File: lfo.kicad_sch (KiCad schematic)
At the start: 3 parts

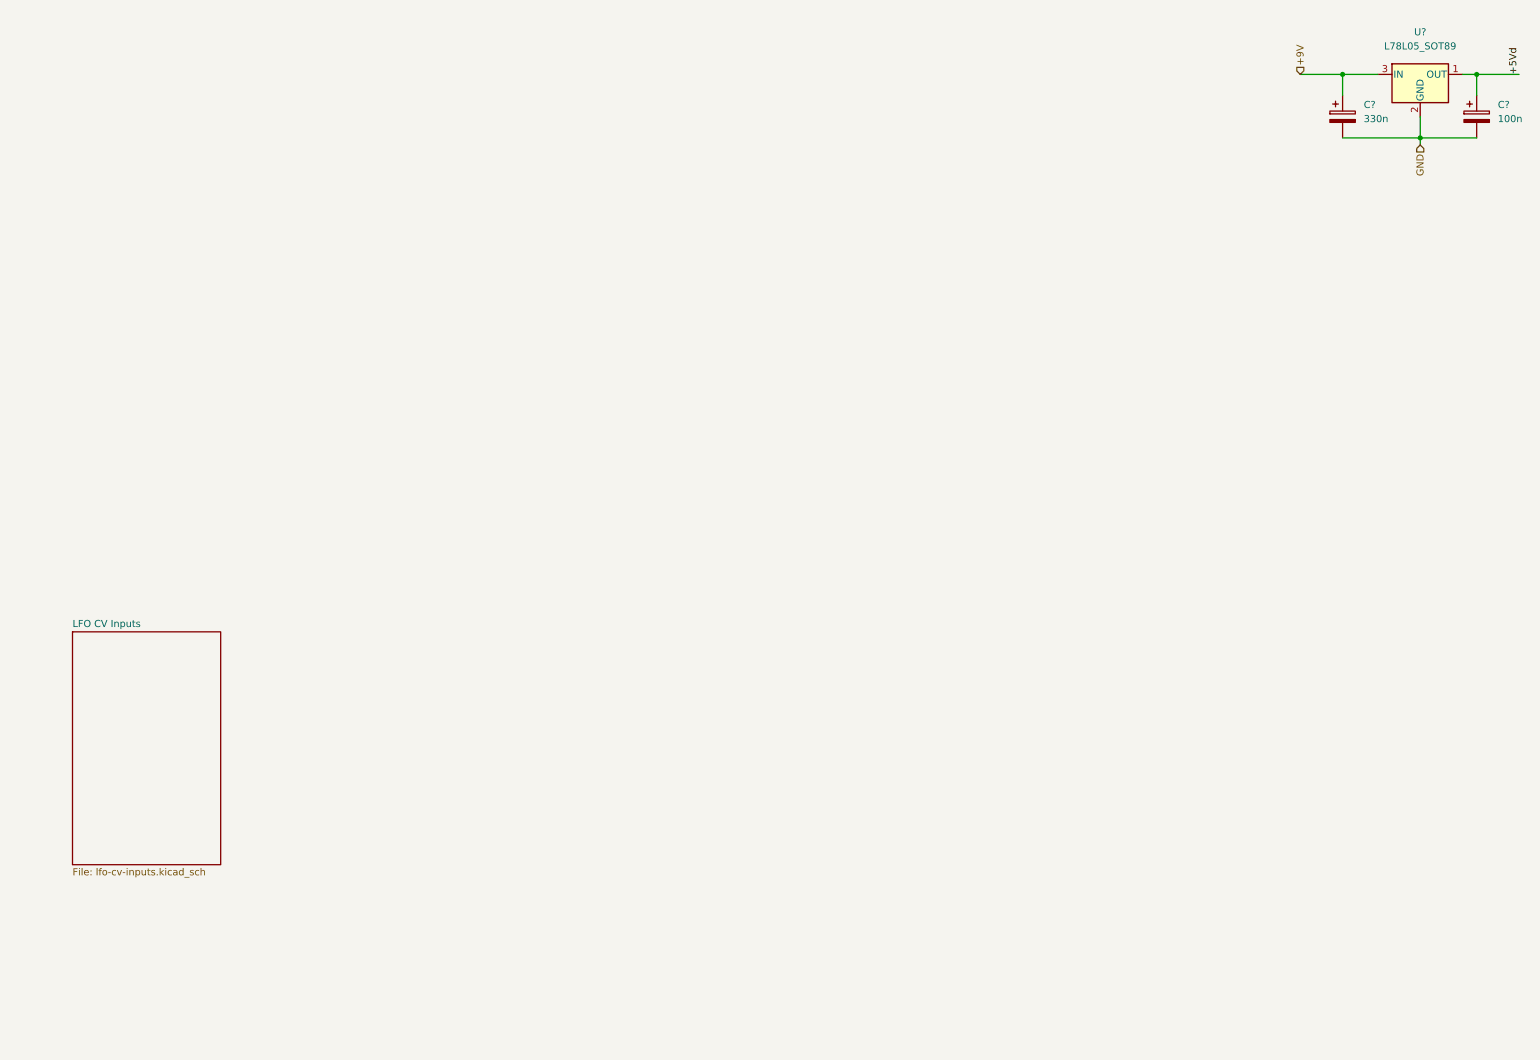
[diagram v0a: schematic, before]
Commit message: LFO schem capture done / replace r2r opamps
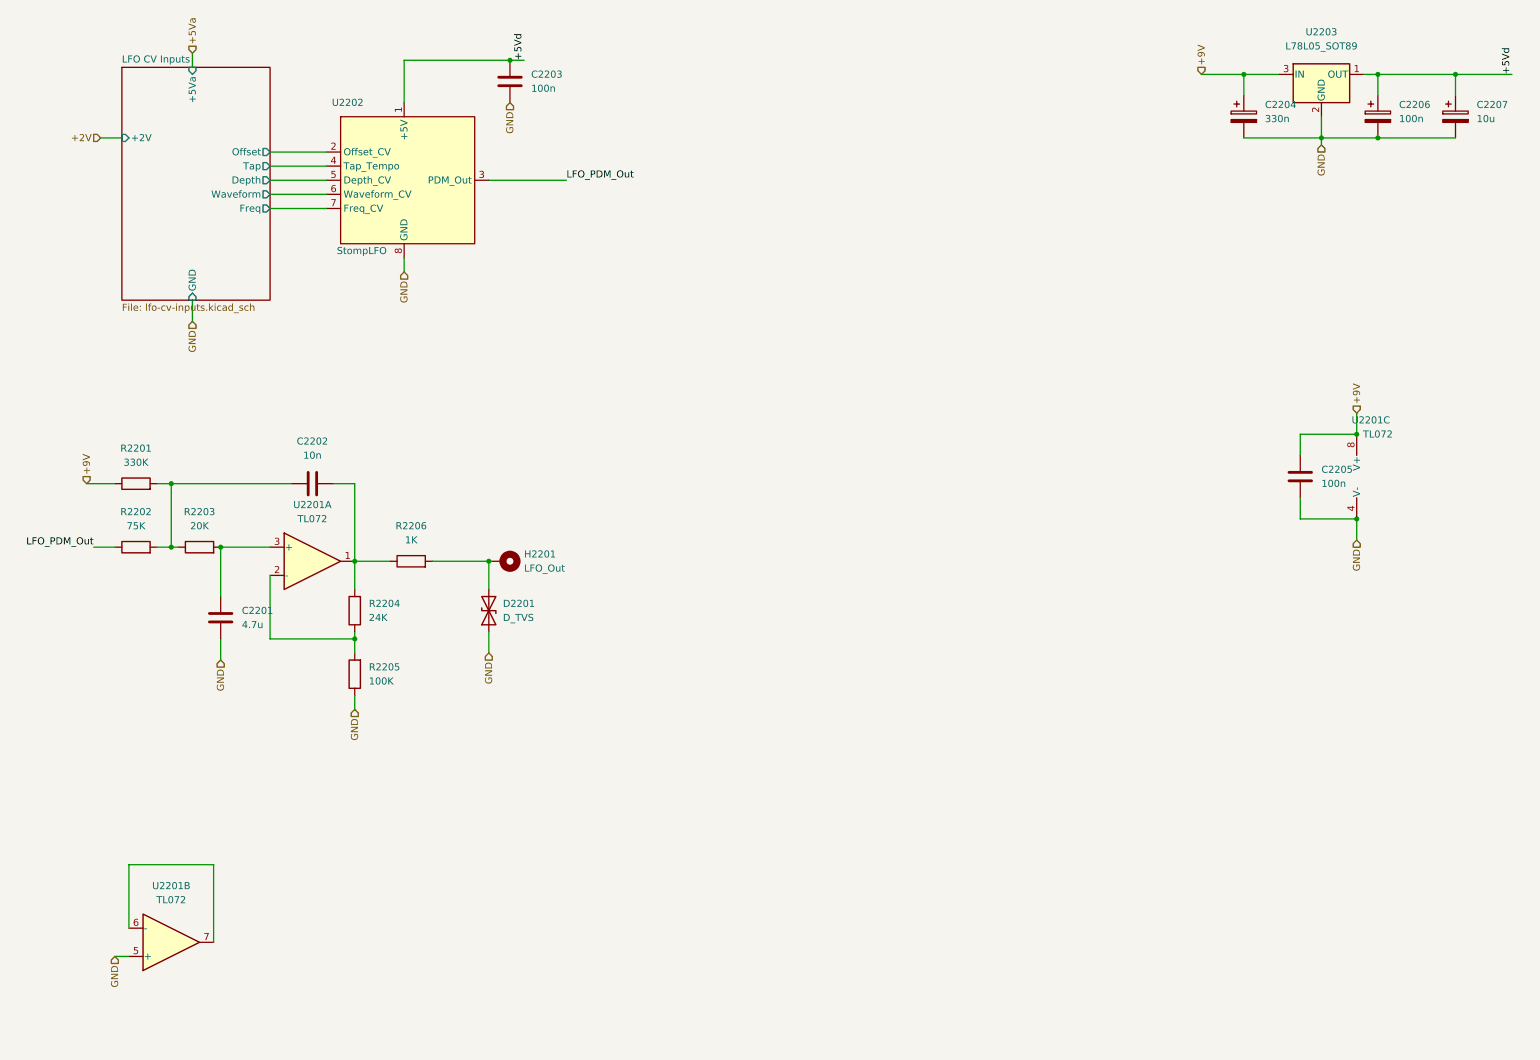
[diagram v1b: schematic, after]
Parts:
- added C2201: 4.7u, Capacitor_SMD:C_0603_1608Metric_Pad1.08x0.95mm_HandSolder, symbol Device:C
- added C2202: 10n, Capacitor_SMD:C_0603_1608Metric_Pad1.08x0.95mm_HandSolder, symbol Device:C
- added C2203, C2205: 100n, Capacitor_SMD:C_0603_1608Metric_Pad1.08x0.95mm_HandSolder, symbol Device:C
- added C2207: 10u, Capacitor_SMD:CP_Elec_4x5.4, symbol Device:C_Polarized
- added D2201: D_TVS, Diode_SMD:D_SOD-323_HandSoldering, symbol Device:D_TVS
- added H2201: LFO_Out, MountingHole:MountingHole_4.3mm_M4_Pad_TopBottom, symbol Mechanical:MountingHole_Pad
- added R2201: 330K, Resistor_SMD:R_0603_1608Metric_Pad0.98x0.95mm_HandSolder, symbol Device:R
- added R2202: 75K, Resistor_SMD:R_0603_1608Metric_Pad0.98x0.95mm_HandSolder, symbol Device:R
- added R2203: 20K, Resistor_SMD:R_0603_1608Metric_Pad0.98x0.95mm_HandSolder, symbol Device:R
- added R2204: 24K, Resistor_SMD:R_0603_1608Metric_Pad0.98x0.95mm_HandSolder, symbol Device:R
- added R2205: 100K, Resistor_SMD:R_0603_1608Metric_Pad0.98x0.95mm_HandSolder, symbol Device:R
- added R2206: 1K, Resistor_SMD:R_0603_1608Metric_Pad0.98x0.95mm_HandSolder, symbol Device:R
- added U2201: TL072, Package_SO:SOIC-8_3.9x4.9mm_P1.27mm, symbol Amplifier_Operational:TL072
- added U2202: StompLFO, Package_DIP:DIP-8_W7.62mm, symbol stomplfo:StompLFO
- gave numbers to parts that had none: 3
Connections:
- net +5Vd: now also C2203.1, C2207.1, U2202.1 (+5V)
- net +9V: now also C2205.1, R2201.1, U2201.8 (V+)
- net GND: now also C2201.2, C2203.2, C2205.2, C2207.2, D2201.1 (A1), R2205.1, U2201.4 (V-), U2201.5 (+), U2202.8 (GND)
- new net: R2204.1, R2205.2, U2201.2 (-)
- new net: C2202.1, R2201.2, R2202.2, R2203.1
- new net: U2201.6 (-), U2201.7
- new net: C2202.2, R2204.2, R2206.1, U2201.1
- new net: D2201.2 (A2), H2201.1, R2206.2
- new net: C2201.1, R2203.2, U2201.3 (+)
- new net LFO CV Inputs/Depth: U2202.5 (Depth_CV)
- new net LFO CV Inputs/Freq: U2202.7 (Freq_CV)
- new net LFO CV Inputs/Offset: U2202.2 (Offset_CV)
- new net LFO CV Inputs/Tap: U2202.4 (Tap_Tempo)
- new net LFO CV Inputs/Waveform: U2202.6 (Waveform_CV)
- new net LFO_PDM_Out: R2202.1, U2202.3 (PDM_Out)
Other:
- sheet LFO CV Inputs ports: added +2V, +5Va, Depth, Freq, GND, Offset, Tap, Waveform; removed none
- moved on the sheet: C2204, C2206, U2203

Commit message: LFO layout down
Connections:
- net GND: now also U2201.3 (+); no longer U2201.5 (+)
- net at R2204.1, R2205.2: now also U2201.6 (-); no longer U2201.2 (-)
- net at C2202.2, R2204.2, R2206.1: now also U2201.7; no longer U2201.1
- net at C2201.1, R2203.2: now also U2201.5 (+); no longer U2201.3 (+)
- new net: U2201.1, U2201.2 (-)
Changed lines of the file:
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@@
     (pin "2")
   )
-  (symbol (lib_id "Amplifier_Operational:TL072") (at 39.37 179.07 0) (mirror x) (unit 2)
+  (symbol (lib_id "Amplifier_Operational:TL072") (at 39.37 179.07 0) (mirror x) (unit 1)
     (in_bom yes) (on_board yes) (fields_autoplaced)
     (property "Reference" "U2201" (id 0) (at 39.37 168.91 0))
@@
     (pin "2")
   )
-  (symbol (lib_id "Amplifier_Operational:TL072") (at 64.77 110.49 0) (unit 1)
+  (symbol (lib_id "Amplifier_Operational:TL072") (at 64.77 110.49 0) (unit 2)
     (in_bom yes) (on_board yes) (fields_autoplaced)
     (property "Reference" "U2201" (id 0) (at 64.77 100.33 0))

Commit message: Relay switch schem capture done
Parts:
- added C2208: 100n, Capacitor_SMD:C_0603_1608Metric_Pad1.08x0.95mm_HandSolder, symbol Device:C
- added C2209: 4.7u, Capacitor_SMD:C_0603_1608Metric_Pad1.08x0.95mm_HandSolder, symbol Device:C
- added R2207, R2208: 20K, Resistor_SMD:R_0603_1608Metric_Pad0.98x0.95mm_HandSolder, symbol Device:R
- added R2209, R2210: 10K, Resistor_SMD:R_0603_1608Metric_Pad0.98x0.95mm_HandSolder, symbol Device:R
- added R2211: 100, Resistor_SMD:R_0603_1608Metric_Pad0.98x0.95mm_HandSolder, symbol Device:R
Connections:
- net +2V: now also C2208.1, C2209.1, R2211.2
- net +5Va: now also R2207.1
- net +9V: now also R2208.1
- net GND: now also C2208.2, C2209.2, R2209.1; no longer U2201.3 (+)
- net at U2201.2 (-): now also R2207.2, R2210.1; no longer U2201.1
- new net: R2210.2, R2211.1, U2201.1
- new net: R2208.2, R2209.2, U2201.3 (+)
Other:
- moved on the sheet: U2201A

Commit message: PSU schem capture done
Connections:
- net +9V: no longer C2204.1, U2203.3 (IN)
- new net +9Vd: C2204.1, U2203.3 (IN)
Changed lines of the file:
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@@
     (effects (font (size 1.27 1.27)) (justify left))
   )
-  (hierarchical_label "+9V" (shape input) (at 224.79 22.86 90)
+  (hierarchical_label "+9Vd" (shape input) (at 224.79 22.86 90)
     (effects (font (size 1.27 1.27)) (justify left))
   )

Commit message: Add JLC parts numbers
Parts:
- C2201, C2209: LCSC (none) -> C380325; Role (none) -> cv-filter
- C2203, C2205: LCSC (none) -> C497032; Role (none) -> ic-bypass
- C2204: LCSC (none) -> C264238; Role (none) -> psu-filter
- C2206: LCSC (none) -> C271438; Role (none) -> psu-filter
- C2207: LCSC (none) -> C294524; Role (none) -> psu-filter
- C2208: LCSC (none) -> C519438; Role (none) -> cv-filter
- D2201: LCSC (none) -> C20936
- R2201: LCSC (none) -> C328354
- R2202: LCSC (none) -> C101185
- R2203, R2207, R2208: LCSC (none) -> C2907011
- R2204: LCSC (none) -> C2930081
- R2205: LCSC (none) -> C14675
- R2206: LCSC (none) -> C2907002
- R2209, R2210: LCSC (none) -> C98220
- R2211: LCSC (none) -> C103197
- U2201: LCSC (none) -> C67473
- U2203: LCSC (none) -> C347258
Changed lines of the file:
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@@
+      (effects (font (size 1.27 1.27)) hide)
+    )
+    (property "LCSC" "C497032" (id 4) (at 100.33 24.13 0)
+      (effects (font (size 1.27 1.27)) hide)
+    )
+    (property "Role" "ic-bypass" (id 5) (at 100.33 24.13 0)
       (effects (font (size 1.27 1.27)) hide)
     )
@@
     )
     (property "Datasheet" "~" (id 3) (at 72.39 130.81 0)
+      (effects (font (size 1.27 1.27)) hide)
+    )
+    (property "LCSC" "C14675" (id 4) (at 72.39 130.81 0)
       (effects (font (size 1.27 1.27)) hide)
     )
@@
       (effects (font (size 1.27 1.27)) hide)
     )
+    (property "LCSC" "C380325" (id 4) (at 99.06 181.61 0)
+      (effects (font (size 1.27 1.27)) hide)
+    )
+    (property "Role" "cv-filter" (id 5) (at 99.06 181.61 0)
+      (effects (font (size 1.27 1.27)) hide)
+    )
     (pin "1")
     (pin "2")
@@
     )
     (property "Datasheet" "~" (id 3) (at 242.57 95.25 0)
+      (effects (font (size 1.27 1.27)) hide)
+    )
+    (property "LCSC" "C497032" (id 4) (at 242.57 95.25 0)
+      (effects (font (size 1.27 1.27)) hide)
+    )
+    (property "Role" "ic-bypass" (id 5) (at 242.57 95.25 0)
       (effects (font (size 1.27 1.27)) hide)
     )
@@
     )
     (property "Datasheet" "~" (id 3) (at 64.77 160.02 0)
+      (effects (font (size 1.27 1.27)) hide)
+    )
+    (property "LCSC" "C98220" (id 4) (at 64.77 160.02 0)
       (effects (font (size 1.27 1.27)) hide)
     )
@@
     )
     (property "Datasheet" "http://www.ti.com/lit/ds/symlink/tl071.pdf" (id 3) (at 255.27 95.25 0)
+      (effects (font (size 1.27 1.27)) hide)
+    )
+    (property "LCSC" "C67473" (id 4) (at 255.27 95.25 0)
       (effects (font (size 1.27 1.27)) hide)
     )
@@
       (effects (font (size 1.27 1.27)) hide)
     )
+    (property "LCSC" "C101185" (id 4) (at 33.02 107.95 0)
+      (effects (font (size 1.27 1.27)) hide)
+    )
     (pin "1")
     (pin "2")
@@
     )
     (property "Datasheet" "http://www.ti.com/lit/ds/symlink/tl071.pdf" (id 3) (at 64.77 173.99 0)
+      (effects (font (size 1.27 1.27)) hide)
+    )
+    (property "LCSC" "C67473" (id 4) (at 64.77 173.99 0)
       (effects (font (size 1.27 1.27)) hide)
     )
@@
       (effects (font (size 1.27 1.27)) hide)
     )
+    (property "LCSC" "C519438" (id 4) (at 86.36 181.61 0)
+      (effects (font (size 1.27 1.27)) hide)
+    )
+    (property "Role" "cv-filter" (id 5) (at 86.36 181.61 0)
+      (effects (font (size 1.27 1.27)) hide)
+    )
     (pin "1")
     (pin "2")
@@
       (effects (font (size 1.27 1.27)) hide)
     )
+    (property "LCSC" "C347258" (id 4) (at 246.38 22.86 0)
+      (effects (font (size 1.27 1.27)) hide)
+    )
     (pin "1")
     (pin "2")
@@
       (effects (font (size 1.27 1.27)) hide)
     )
+    (property "LCSC" "C2907011" (id 4) (at 49.53 181.61 0)
+      (effects (font (size 1.27 1.27)) hide)
+    )
     (pin "1")
     (pin "2")
@@
     )
     (property "Datasheet" "~" (id 3) (at 270.51 30.48 0)
+      (effects (font (size 1.27 1.27)) hide)
+    )
+    (property "LCSC" "C294524" (id 4) (at 270.51 30.48 0)
+      (effects (font (size 1.27 1.27)) hide)
+    )
+    (property "Role" "psu-filter" (id 5) (at 270.51 30.48 0)
       (effects (font (size 1.27 1.27)) hide)
     )
@@
       (effects (font (size 1.27 1.27)) hide)
     )
+    (property "LCSC" "C2907002" (id 4) (at 82.55 110.49 0)
+      (effects (font (size 1.27 1.27)) hide)
+    )
     (pin "1")
     (pin "2")
@@
       (effects (font (size 1.27 1.27)) hide)
     )
+    (property "LCSC" "C2907011" (id 4) (at 49.53 171.45 0)
+      (effects (font (size 1.27 1.27)) hide)
+    )
     (pin "1")
     (pin "2")
@@
     )
     (property "Datasheet" "~" (id 3) (at 54.61 185.42 0)
+      (effects (font (size 1.27 1.27)) hide)
+    )
+    (property "LCSC" "C98220" (id 4) (at 54.61 185.42 0)
       (effects (font (size 1.27 1.27)) hide)
     )
@@
       (effects (font (size 1.27 1.27)) hide)
     )
+    (property "LCSC" "C2907011" (id 4) (at 44.45 107.95 0)
+      (effects (font (size 1.27 1.27)) hide)
+    )
     (pin "1")
     (pin "2")
@@
       (effects (font (size 1.27 1.27)) hide)
     )
+    (property "LCSC" "C380325" (id 4) (at 48.26 120.65 0)
+      (effects (font (size 1.27 1.27)) hide)
+    )
+    (property "Role" "cv-filter" (id 5) (at 48.26 120.65 0)
+      (effects (font (size 1.27 1.27)) hide)
+    )
     (pin "1")
     (pin "2")
@@
       (effects (font (size 1.27 1.27)) hide)
     )
+    (property "LCSC" "C264238" (id 4) (at 232.41 30.48 0)
+      (effects (font (size 1.27 1.27)) hide)
+    )
+    (property "Role" "psu-filter" (id 5) (at 232.41 30.48 0)
+      (effects (font (size 1.27 1.27)) hide)
+    )
     (pin "1")
     (pin "2")
@@
     )
     (property "Datasheet" "~" (id 3) (at 96.52 119.38 0)
+      (effects (font (size 1.27 1.27)) hide)
+    )
+    (property "LCSC" "C20936" (id 4) (at 96.52 119.38 0)
       (effects (font (size 1.27 1.27)) hide)
     )
@@
       (effects (font (size 1.27 1.27)) hide)
     )
+    (property "LCSC" "C328354" (id 4) (at 33.02 96.52 0)
+      (effects (font (size 1.27 1.27)) hide)
+    )
     (pin "1")
     (pin "2")
@@
     )
     (property "Datasheet" "http://www.ti.com/lit/ds/symlink/tl071.pdf" (id 3) (at 64.77 110.49 0)
+      (effects (font (size 1.27 1.27)) hide)
+    )
+    (property "LCSC" "C67473" (id 4) (at 64.77 110.49 0)
       (effects (font (size 1.27 1.27)) hide)
     )
@@
       (effects (font (size 1.27 1.27)) hide)
     )
+    (property "LCSC" "C2930081" (id 4) (at 72.39 119.38 0)
+      (effects (font (size 1.27 1.27)) hide)
+    )
     (pin "1")
     (pin "2")
@@
       (effects (font (size 1.27 1.27)) hide)
     )
+    (property "LCSC" "C103197" (id 4) (at 78.74 173.99 0)
+      (effects (font (size 1.27 1.27)) hide)
+    )
     (pin "1")
     (pin "2")
@@
       (effects (font (size 1.27 1.27)) hide)
     )
+    (property "LCSC" "C271438" (id 4) (at 256.54 30.48 0)
+      (effects (font (size 1.27 1.27)) hide)
+    )
+    (property "Role" "psu-filter" (id 5) (at 256.54 30.48 0)
+      (effects (font (size 1.27 1.27)) hide)
+    )
